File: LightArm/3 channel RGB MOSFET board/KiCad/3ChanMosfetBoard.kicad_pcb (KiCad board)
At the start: 2 copper layers, 20 parts, among them IC1 MOC3010M, IC2 MOC3010M, IC3 MOC3010M, K1 CONN_3, P1 PWM, P2 CONN_2, P3 CONN_2, P4 CONN_2, Q1 C_MOS, Q2 C_MOS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

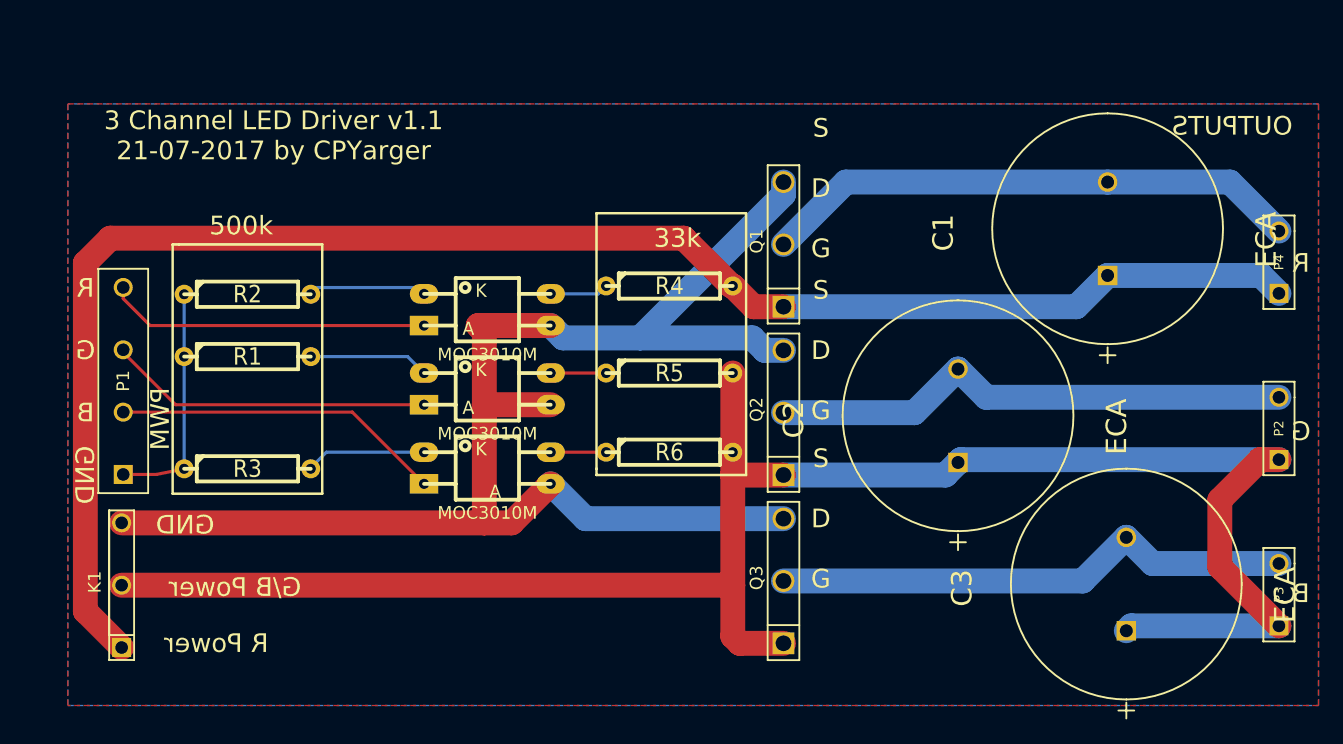
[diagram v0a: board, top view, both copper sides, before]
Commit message: update light and motor boards
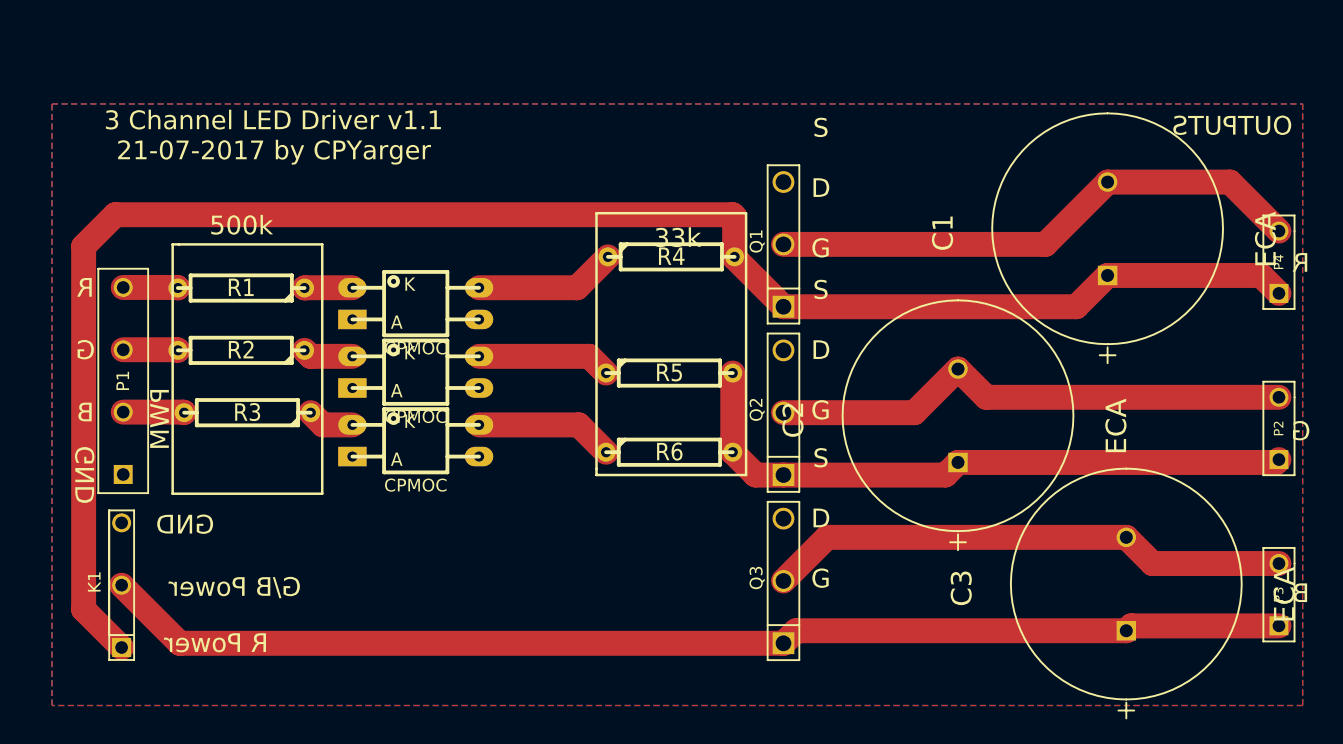
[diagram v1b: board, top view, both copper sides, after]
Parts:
- IC1, IC2, IC3: value MOC3010M -> CPMOC; footprint OPTORESISTOR_NSL-32 -> CPDIP4
- moved IC3 6.15 mm to (176.5, 152.8)
- moved IC2 5.90 mm to (176.5, 147.2)
- moved IC1 5.77 mm to (176.5, 141.8)
- moved R1 5.52 mm to (162.5, 140.5), turned to 180 degrees
- moved R2 4.53 mm to (162.5, 145.5), turned to 180 degrees
- moved R3 4.50 mm to (163.0, 150.5), turned to 180 degrees
- moved R4 2.34 mm to (197.0, 138.0)
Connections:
- IC1 pad 1: N-0000013 -> N-000006
- IC1 pad 2: N-000007 -> N-000008
- IC1 pad 3: (no net) -> N-000007
- IC2 pad 1: N-0000012 (its old number) -> N-000004
- IC2 pad 2: N-000005 -> N-000008
- IC2 pad 3: (no net) -> N-000009
- IC3 pad 1: N-0000011 (its old number) -> N-000005
- IC3 pad 2: N-000003 (its old number) -> N-000008
- IC3 pad 3: (no net) -> N-0000010
- P1 pad 1: N-000006 -> N-000008
- P1 pad 2: N-0000011 (its old number) -> N-0000013
- P1 pad 3: N-0000012 (its old number) -> N-0000014
- P1 pad 4: N-0000013 -> N-0000015
- R1 pad 2: N-000005 -> N-0000015
- R2 pad 1: N-000006 -> N-000004
- R2 pad 2: N-000007 -> N-0000014
- R3 pad 1: N-000006 -> N-000005
- R3 pad 2: N-000003 (its old number) -> N-0000013
- R4 pad 1: N-000009 -> N-000007
- R5 pad 1: N-000008 -> N-000009
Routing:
- net N-0000016: track 119.5 -> 0.00 mm
- net N-0000011 (its old number): track 26.5 -> 0.00 mm
- net N-0000012 (its old number): track 26.1 -> 0.00 mm
- net N-0000013: track 25.9 -> 4.90 mm
- net N-000006: track 19.0 -> 3.85 mm
- net N-0000010: track 0.00 -> 11.1 mm
- net N-000003 (its old number): track 9.68 -> 0.00 mm
- net (no net): track 8.89 -> 0.00 mm
- net N-000009: track 4.71 -> 10.7 mm
- net N-000005: track 9.63 -> 3.75 mm
- net N-0000012: track 132.5 -> 137.0 mm
- net N-0000015: track 0.00 -> 4.40 mm
- net N-0000014: track 0.00 -> 4.40 mm
- net N-000004: track 0.00 -> 4.04 mm
- net N-0000011: track 149.3 -> 146.8 mm
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- added copper zone on F.Cu, net N-0000016
- added copper zone on B.Cu, net N-000008
- removed copper zone on B.Cu, net N-000001
- removed copper zone on F.Cu, net N-000001
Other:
- net class Default: trace_width 0.254 -> 1.9

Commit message: updating various changes in codebase , adding in new esp32 directory for code running on the esp32
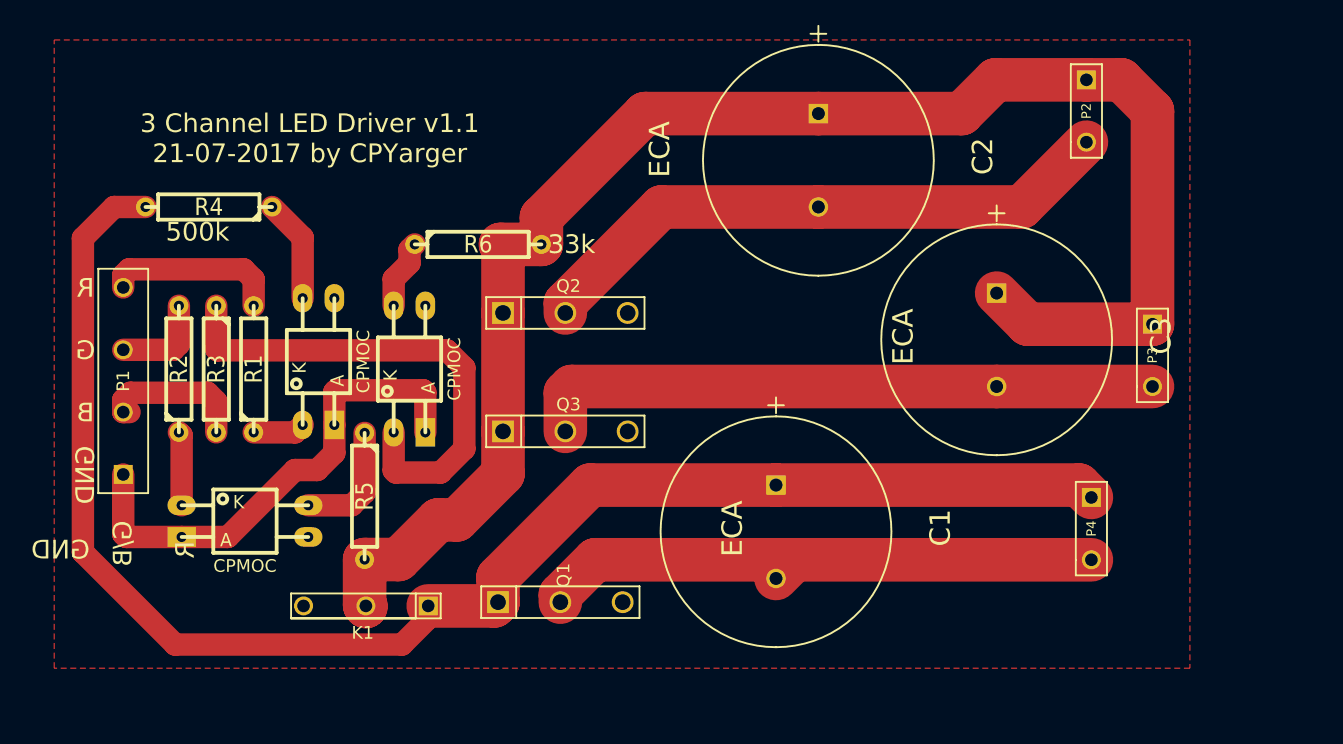
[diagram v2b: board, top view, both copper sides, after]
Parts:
- moved C1 41.5 mm to (205.4, 163.8), turned to 270 degrees
- moved R4 37.3 mm to (159.9, 134.0), turned to 180 degrees
- moved Q1 33.8 mm to (188.1, 165.7), turned to 0 degrees
- moved P2 29.8 mm to (230.3, 126.3), turned to 270 degrees
- moved R5 26.4 mm to (172.4, 157.2), turned to 270 degrees
- moved P4 26.1 mm to (230.7, 159.8), turned to 270 degrees
- moved R6 22.7 mm to (181.5, 137.0)
- moved P3 21.7 mm to (235.6, 145.9), turned to 270 degrees
- moved Q3 21.2 mm to (188.5, 152.0), turned to 0 degrees
- moved K1 19.7 mm to (172.5, 166.0), turned to 180 degrees
- moved Q2 19.2 mm to (188.5, 142.5), turned to 0 degrees
- moved IC2 18.2 mm to (162.8, 159.2)
- moved C2 17.2 mm to (208.8, 134.0), turned to 270 degrees
- moved C3 16.0 mm to (223.1, 148.4), turned to 270 degrees
- moved IC1 9.08 mm to (168.7, 146.4), turned to 90 degrees
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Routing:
- net N-000008: track 0.00 -> 40.1 mm
- net N-000005: track 3.75 -> 40.1 mm
- net N-0000011: track 146.8 -> 127.2 mm
- net N-0000012: track 137.0 -> 122.7 mm
- net N-0000015: track 4.40 -> 14.1 mm
- net N-000002: track 42.1 -> 50.4 mm
- net N-0000013: track 4.90 -> 12.0 mm
- net N-000001: track 42.1 -> 47.9 mm
- net N-0000010: track 11.1 -> 5.62 mm
- net N-0000014: track 4.40 -> 7.74 mm
- net N-000003: track 43.4 -> 46.5 mm
- net N-000007: track 11.4 -> 8.33 mm
- net N-000004: track 4.04 -> 5.94 mm
- net N-000009: track 10.7 -> 9.73 mm
- removed copper zone on B.Cu, net N-000008
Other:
- net class Default: clearance 0.254 -> 0.3; trace_width 1.9 -> 3.5
- net class HP: clearance 0.254 -> 0.3; trace_width 2 -> 3.5
- rule pad_to_mask_clearance: 0 -> 1
- rule trace_clearance: 0.254 -> 0.3
- board text added: "G/B"
- board text removed: "G/B Power"
- board text removed: "OUTPUTS"
- board text removed: "PWM"
- board text removed: "R Power"
- board text removed: "S D G"
